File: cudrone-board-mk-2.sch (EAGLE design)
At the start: 137 parts, among them U1 EDISON_CONNECTOR_FULLMOUNTING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, U10 A2235-H, U11 FTS31XS-U, U12 BNO055, U13 DSPIC33EP512MU810-X_PF, U2 FTS31XS-U, U4 TPS62065, U5 USD-SOCKETNEW, U6 TXB0108, U8 PCA9306, U9 PCA9306

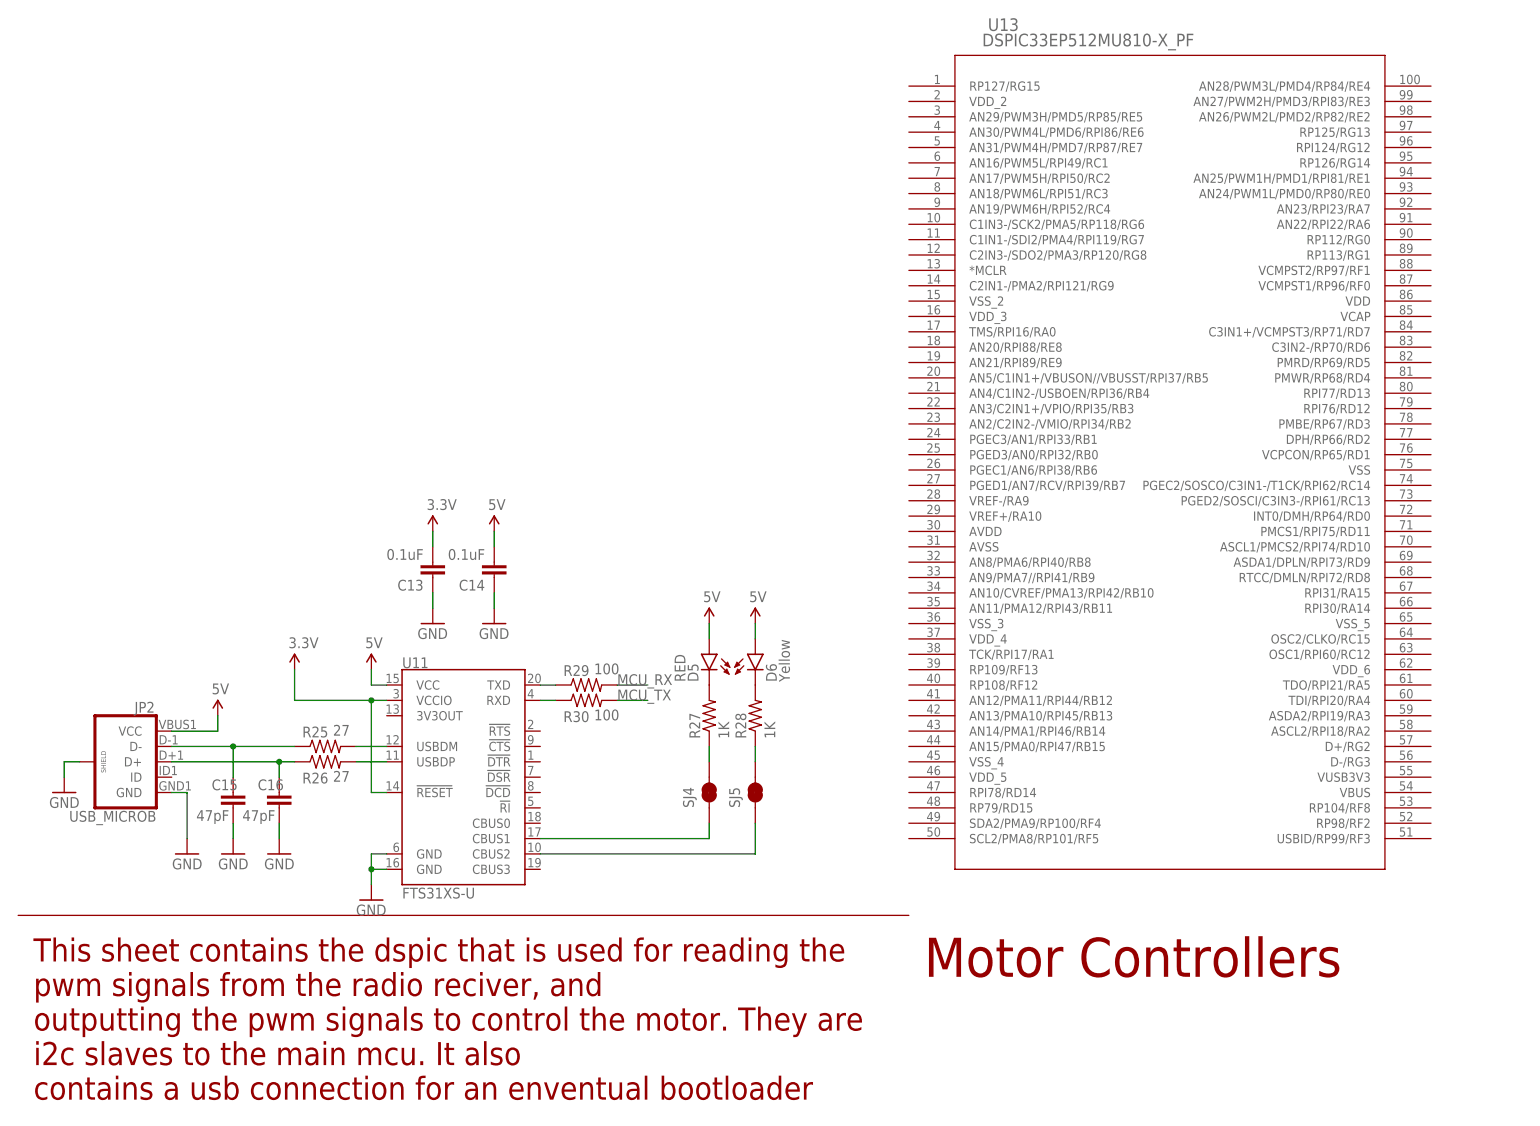
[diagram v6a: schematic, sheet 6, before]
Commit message: Added decoupling caps to mcu and isp pins
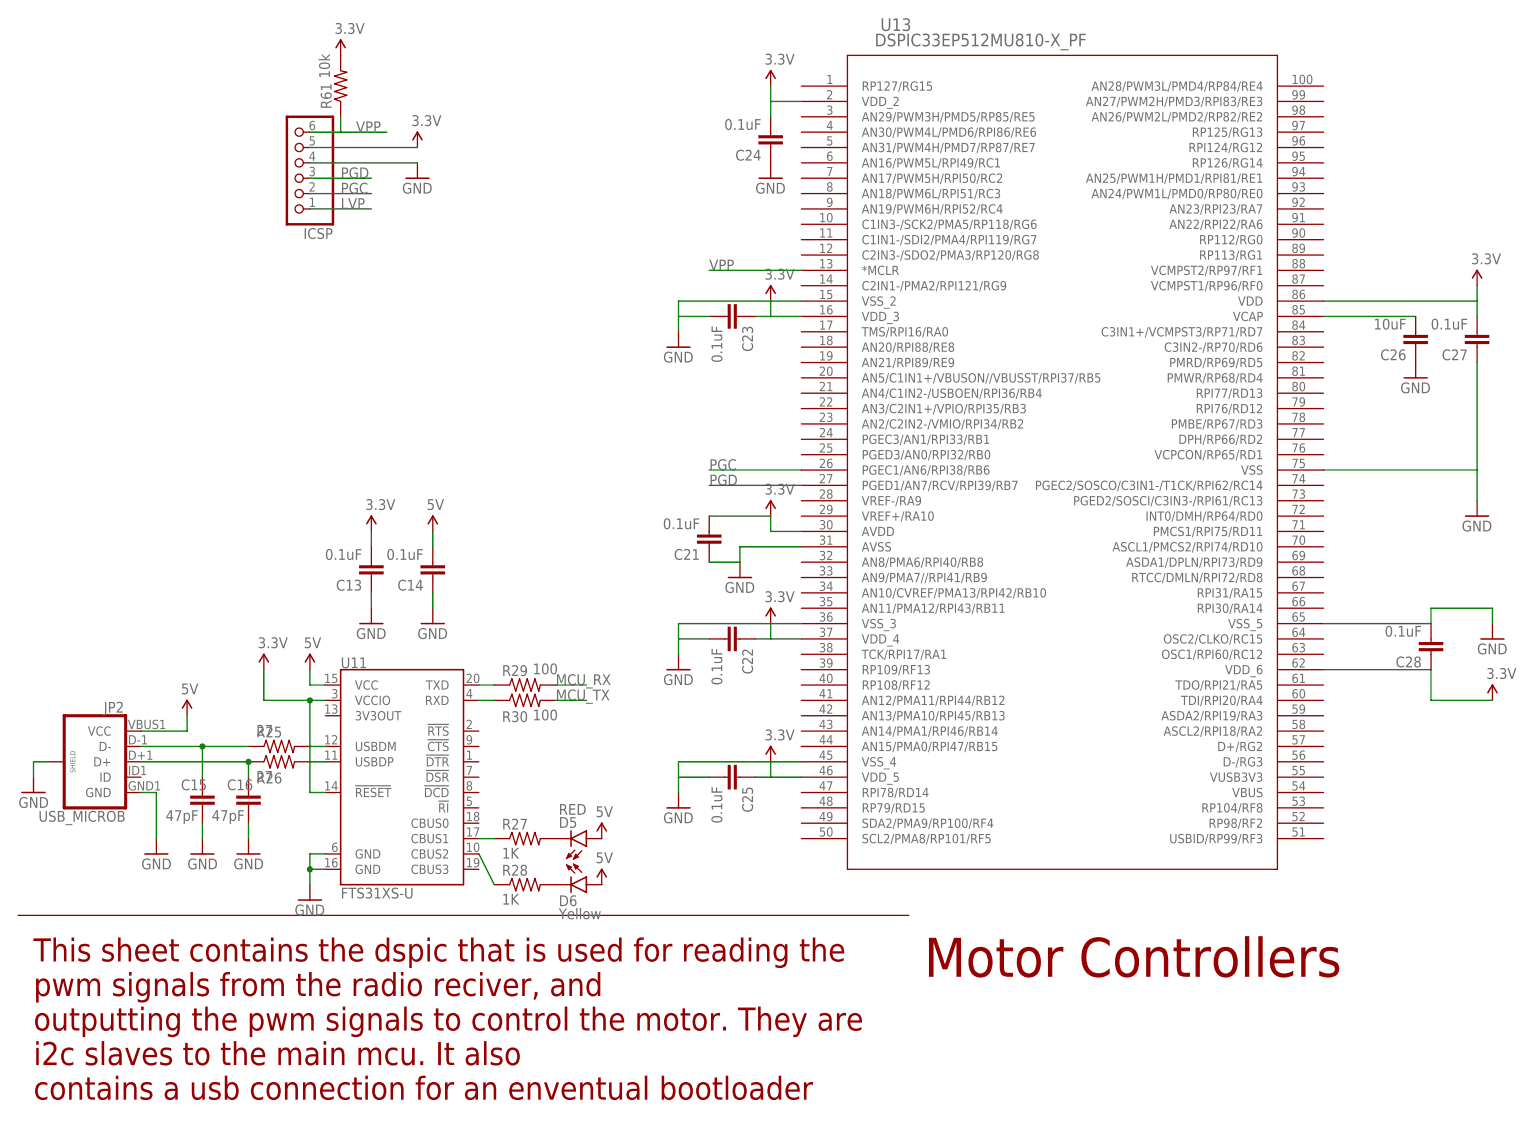
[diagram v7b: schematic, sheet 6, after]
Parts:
- removed SJ4, SJ5: JUMPER-PAD-2-NC_BY_TRACE, SparkFun-Passives:JUMPER-PAD-2-NC_BY_TRACE
- added C21, C22, C23, C24, C25, C27, C28: 0.1uF, SparkFun-Capacitors:0.1UF-25V(+80/-20%)(0603)
- added C26: 10uF, SparkFun-Capacitors:0.1UF-25V(+80/-20%)(0603)
- added ICSP: (no value), pinhead:PINHD-1X6/90
- added R61: 10k, SparkFun-Resistors:27OHM1/10W1%(0603)
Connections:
- removed net N$33: R28.1, SJ5.2
- new net LVP: ICSP.1
- new net PGC: ICSP.2, U13.PGEC1/AN6/RPI38/RB6
- new net PGD: ICSP.3, U13.PGED1/AN7/RCV/RPI39/RB7
- new net VPP: ICSP.6, R61.1, U13.*MCLR
- net 3.3V: now also C21.2, C22.1, C23.1, C24.2, C25.1, C27.2, C28.1, ICSP.5, R61.2, U13.AVDD, U13.VDD, U13.VDD_2, U13.VDD_3, U13.VDD_4, U13.VDD_5, U13.VDD_6
- net GND: now also C21.1, C22.2, C23.2, C24.1, C25.2, C26.1, C27.1, C28.2, ICSP.4, U13.AVSS, U13.VSS, U13.VSS_2, U13.VSS_3, U13.VSS_4, U13.VSS_5
- net N$30: now also C26.2, U13.VCAP; no longer SJ4.1, U11.CBUS1
- net N$31: now also R28.1; no longer SJ5.1
- net N$32: now also U11.CBUS1; no longer SJ4.2
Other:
- moved on the sheet: C13, C14, C15, C16, C17, C19, C20, D5, D6, JP2, R25, R26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

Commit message: Connected i2c busses
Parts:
- removed SJ3: JUMPER-PAD-2-NC_BY_TRACE, SparkFun-Passives:JUMPER-PAD-2-NC_BY_TRACE
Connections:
- removed net I2C0_SCL: U$4.SCL, U$5.SCL, U12.COM1
- removed net I2C0_SDA: U$4.SDA, U$5.SDA, U12.COM0
- removed net N$13: R5.1, SJ3.2
- net GND: now also R5.1; no longer SJ3.1
- net I2C_1_SCL: now also U$4.SCL, U$5.SCL, U12.COM1, U13.ASCL1/PMCS2/RPI74/RD10
- net I2C_1_SDA: now also U$4.SDA, U$5.SDA, U12.COM0, U13.ASDA1/DPLN/RPI73/RD9
- net I2C_2_SCL: now also U13.ASCL2/RPI18/RA2
- net I2C_2_SDA: now also U13.ASDA2/RPI19/RA3
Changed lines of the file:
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@@
 <part name="FRAME9" library="frames" deviceset="LETTER_L" device=""/>
 <part name="U1" library="SparkFun-Boards" deviceset="EDISON_CONNECTOR_FULL" device="MOUNTING_HOLES"/>
-<part name="GND3" library="supply1" deviceset="GND" device=""/>
+<part name="GND3" library="supply1" library_urn="urn:adsk.eagle:library:371" deviceset="GND" device=""/>
 <part name="BAT_BACKUP" library="SparkFun-Electromechanical" deviceset="BATTERY" device="12MM" value="RTC backup battery"/>
 <part name="GND1" library="SparkFun-Aesthetics" deviceset="GND" device=""/>
@@
 <part name="D3" library="SparkFun-LED" deviceset="LED-BLUE" device="0603" value="BLUE"/>
 <part name="GND12" library="SparkFun-Aesthetics" deviceset="GND" device=""/>
-<part name="SJ3" library="SparkFun-Passives" deviceset="JUMPER-PAD-2-NC_BY_TRACE" device=""/>
 <part name="C6" library="SparkFun-Capacitors" deviceset="22UF-6.3V-20%(0805)" device="" value="22uF"/>
 <part name="GND14" library="SparkFun-Aesthetics" deviceset="GND" device=""/>
@@
 <part name="GND55" library="SparkFun-Aesthetics" deviceset="GND" device=""/>
 <part name="GND56" library="SparkFun-Aesthetics" deviceset="GND" device=""/>
-<part name="ICSP" library="pinhead" deviceset="PINHD-1X6" device="/90"/>
+<part name="ICSP" library="pinhead" library_urn="urn:adsk.eagle:library:325" deviceset="PINHD-1X6" device="/90"/>
 <part name="GND57" library="SparkFun-Aesthetics" deviceset="GND" device=""/>
 <part name="SUPPLY100" library="SparkFun-Aesthetics" deviceset="3.3V" device=""/>
@@
 <instance part="D3" gate="G$1" x="149.86" y="162.56"/>
 <instance part="GND12" gate="1" x="149.86" y="127"/>
-<instance part="SJ3" gate="G$1" x="149.86" y="137.16" smashed="yes" rot="R90">
-<attribute name="NAME" x="147.32" y="134.62" size="1.778" layer="95" rot="R90"/>
-</instance>
 <instance part="C6" gate="G$1" x="137.16" y="147.32"/>
 <instance part="GND14" gate="1" x="137.16" y="132.08"/>
@@
 <segment>
 <pinref part="GND12" gate="1" pin="GND"/>
-<pinref part="SJ3" gate="G$1" pin="1"/>
-<wire x1="149.86" y1="132.08" x2="149.86" y2="129.54" width="0.1524" layer="91"/>
+<pinref part="R5" gate="G$1" pin="1"/>
+<wire x1="149.86" y1="144.78" x2="149.86" y2="129.54" width="0.1524" layer="91"/>
 </segment>
 <segment>
@@
 </segment>
 </net>
-<net name="N$13" class="0">
-<segment>
-<pinref part="R5" gate="G$1" pin="1"/>
-<pinref part="SJ3" gate="G$1" pin="2"/>
-<wire x1="149.86" y1="142.24" x2="149.86" y2="144.78" width="0.1524" layer="91"/>
-</segment>
-</net>
 <net name="N$17" class="0">
 <segment>
@@
 </segment>
 </net>
+<net name="I2C_1_SDA" class="0">
+<segment>
+<pinref part="U13" gate="A" pin="ASDA1/DPLN/RPI73/RD9"/>
+<wire x1="215.9" y1="93.98" x2="228.6" y2="93.98" width="0.1524" layer="91"/>
+<label x="215.9" y="93.98" size="1.778" layer="95"/>
+</segment>
+</net>
+<net name="I2C_1_SCL" class="0">
+<segment>
+<pinref part="U13" gate="A" pin="ASCL1/PMCS2/RPI74/RD10"/>
+<wire x1="215.9" y1="96.52" x2="228.6" y2="96.52" width="0.1524" layer="91"/>
+<label x="215.9" y="96.52" size="1.778" layer="95"/>
+</segment>
+</net>
+<net name="I2C_2_SDA" class="0">
+<segment>
+<pinref part="U13" gate="A" pin="ASDA2/RPI19/RA3"/>
+<wire x1="215.9" y1="68.58" x2="228.6" y2="68.58" width="0.1524" layer="91"/>
+<label x="215.9" y="68.58" size="1.778" layer="95"/>
+</segment>
+</net>
+<net name="I2C_2_SCL" class="0">
+<segment>
+<pinref part="U13" gate="A" pin="ASCL2/RPI18/RA2"/>
+<wire x1="215.9" y1="66.04" x2="228.6" y2="66.04" width="0.1524" layer="91"/>
+<label x="215.9" y="66.04" size="1.778" layer="95"/>
+</segment>
+</net>
 </nets>
 </sheet>
@@
 <wire x1="7.62" y1="149.86" x2="25.4" y2="149.86" width="0.1524" layer="91"/>
 </segment>
+<segment>
+<wire x1="142.24" y1="147.32" x2="160.02" y2="147.32" width="0.1524" layer="91"/>
+<label x="142.24" y="147.32" size="1.778" layer="95"/>
+<pinref part="U12" gate="G$1" pin="COM1"/>
+</segment>
+<segment>
+<wire x1="170.18" y1="96.52" x2="154.94" y2="96.52" width="0.1524" layer="91"/>
+<label x="154.94" y="96.52" size="1.778" layer="95"/>
+<pinref part="U$4" gate="G$1" pin="SCL"/>
+</segment>
+<segment>
+<wire x1="172.72" y1="58.42" x2="157.48" y2="58.42" width="0.1524" layer="91"/>
+<label x="157.48" y="58.42" size="1.778" layer="95"/>
+<pinref part="U$5" gate="G$1" pin="SCL"/>
+</segment>
 </net>
 <net name="I2C_1_SDA" class="0">
@@
 <label x="7.62" y="147.32" size="1.27" layer="95"/>
 </segment>
+<segment>
+<wire x1="142.24" y1="149.86" x2="160.02" y2="149.86" width="0.1524" layer="91"/>
+<label x="142.24" y="149.86" size="1.778" layer="95"/>
+<pinref part="U12" gate="G$1" pin="COM0"/>
+</segment>
+<segment>
+<wire x1="170.18" y1="101.6" x2="154.94" y2="101.6" width="0.1524" layer="91"/>
+<label x="154.94" y="101.6" size="1.778" layer="95"/>
+<pinref part="U$4" gate="G$1" pin="SDA"/>
+</segment>
+<segment>
+<wire x1="172.72" y1="63.5" x2="157.48" y2="63.5" width="0.1524" layer="91"/>
+<label x="157.48" y="63.5" size="1.778" layer="95"/>
+<pinref part="U$5" gate="G$1" pin="SDA"/>
+</segment>
 </net>
 <net name="GP19_I2C_1_SCL" class="0">
@@
 </segment>
 </net>
-<net name="I2C0_SCL" class="1">
-<segment>
-<wire x1="170.18" y1="96.52" x2="154.94" y2="96.52" width="0.1524" layer="91"/>
-<label x="154.94" y="96.52" size="1.778" layer="95"/>
-<pinref part="U$4" gate="G$1" pin="SCL"/>
-</segment>
-<segment>
-<wire x1="142.24" y1="147.32" x2="160.02" y2="147.32" width="0.1524" layer="91"/>
-<label x="142.24" y="147.32" size="1.778" layer="95"/>
-<pinref part="U12" gate="G$1" pin="COM1"/>
-</segment>
-<segment>
-<wire x1="172.72" y1="58.42" x2="157.48" y2="58.42" width="0.1524" layer="91"/>
-<label x="157.48" y="58.42" size="1.778" layer="95"/>
-<pinref part="U$5" gate="G$1" pin="SCL"/>
-</segment>
-</net>
-<net name="I2C0_SDA" class="1">
-<segment>
-<wire x1="170.18" y1="101.6" x2="154.94" y2="101.6" width="0.1524" layer="91"/>
-<label x="154.94" y="101.6" size="1.778" layer="95"/>
-<pinref part="U$4" gate="G$1" pin="SDA"/>
-</segment>
-<segment>
-<wire x1="142.24" y1="149.86" x2="160.02" y2="149.86" width="0.1524" layer="91"/>
-<label x="142.24" y="149.86" size="1.778" layer="95"/>
-<pinref part="U12" gate="G$1" pin="COM0"/>
-</segment>
-<segment>
-<wire x1="172.72" y1="63.5" x2="157.48" y2="63.5" width="0.1524" layer="91"/>
-<label x="157.48" y="63.5" size="1.778" layer="95"/>
-<pinref part="U$5" gate="G$1" pin="SDA"/>
-</segment>
-</net>
 <net name="NINT" class="0">
 <segment>
@@
 which will not be processed correctly with this version.
 </note>
+<note version="8.2" severity="warning">
+Since Version 8.2, Eagle supports online libraries. The ids
+of those online libraries will not be understood (or retained)
+with this version.
+</note>
 </compatibility>
